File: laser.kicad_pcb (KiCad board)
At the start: 2 copper layers, 74 x 32 mm, 40 parts, among them J1 Conn_01x04_Socket, J2 Conn_02x04_Counter_Clockwise, J3 Conn_01x02_Pin, J4 Conn_01x02_Socket, J5 Conn_01x01_Pin, J6 Conn_01x01_Pin, J7 Conn_01x01_Pin, J8 Conn_01x01_Pin, J9 Conn_01x01_Pin, U1 MCP6002-xP

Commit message: Updated PCB board
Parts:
- D1, D2: moved to B.Cu
- moved R1 138.7 mm to (158.7, 89.4), turned to -90 degrees
- moved R12 131.8 mm to (162.1, 96.8)
- moved R2 120.6 mm to (133.9, 101.9), turned to 180 degrees
- moved C11 118.0 mm to (149.3, 119.7)
- moved D2 111.6 mm to (163.7, 90.0)
- moved R3 108.6 mm to (122.2, 101.9), turned to 180 degrees
- moved J2 103.2 mm to (154.0, 82.0), turned to -90 degrees
- moved J1 98.4 mm to (146.4, 95.0), turned to 90 degrees
- moved C4 97.1 mm to (126.2, 89.9), turned to -90 degrees
- moved C3 96.5 mm to (118.6, 95.3), turned to 90 degrees
- moved C2 78.8 mm to (131.4, 80.0), turned to 180 degrees
- moved U1 75.6 mm to (139.3, 69.3), turned to 90 degrees
- moved C1 74.0 mm to (120.1, 80.2), turned to 180 degrees
- moved D1 69.0 mm to (132.7, 90.0)
- moved J9 67.7 mm to (76.9, 116.6)
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
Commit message: Updated PCB
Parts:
- moved R6 118.8 mm to (174.3, 104.4)
- moved R10 102.9 mm to (153.8, 137.2), turned to 180 degrees
- moved R11 95.9 mm to (141.8, 151.2)
- moved C10 94.1 mm to (154.4, 145.8), turned to -90 degrees
- moved C6 90.2 mm to (165.4, 104.3)
- moved J9 89.0 mm to (164.5, 101.0)
- moved R8 88.6 mm to (134.3, 137.4), turned to 180 degrees
- moved R9 73.8 mm to (119.1, 138.2), turned to 180 degrees
- moved J8 68.2 mm to (145.9, 132.0)
- moved J7 65.6 mm to (91.4, 138.6)
- moved C9 64.5 mm to (97.8, 132.8)
- moved J4 64.4 mm to (164.6, 95.5)
- moved C8 60.4 mm to (127.9, 133.0)
- moved C13 52.1 mm to (127.7, 127.3)
- moved R7 40.7 mm to (65.3, 130.3), turned to 180 degrees
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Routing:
- added copper zone on F.Cu, net GND

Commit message: Connect all cables
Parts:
- moved R13 93.2 mm to (157.9, 103.5)
- moved J7 91.4 mm to (176.0, 104.0)
- moved C7 91.4 mm to (155.0, 97.0), turned to -90 degrees
- moved R7 90.8 mm to (152.0, 103.3), turned to 90 degrees
- moved R5 87.9 mm to (142.0, 104.1), turned to 90 degrees
- moved C12 81.8 mm to (171.5, 103.0), turned to 90 degrees
- moved C9 74.1 mm to (164.5, 100.5), turned to 180 degrees
- moved C10 69.5 mm to (141.5, 77.5)
- moved C5 65.8 mm to (138.0, 98.0), turned to -90 degrees
- moved R8 64.9 mm to (171.9, 84.5)
- moved R4 64.9 mm to (116.5, 103.8), turned to 90 degrees
- moved R11 64.8 mm to (138.5, 86.5), turned to -90 degrees
- moved C8 64.2 mm to (165.5, 81.0)
- moved C13 62.6 mm to (165.6, 77.5)
- moved R9 57.0 mm to (158.5, 97.0), turned to 0 degrees
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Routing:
- net GND: track 0.00 -> 120.8 mm
- net Net-(J6-Pin_1): track 0.00 -> 77.5 mm
- net +3.3V: track 0.00 -> 76.3 mm
- net /vgnd: track 0.00 -> 72.4 mm
- net Net-(D2-A): track 0.00 -> 49.7 mm
- net Net-(J8-Pin_1): track 0.00 -> 48.5 mm
- net Net-(J7-Pin_1): track 0.00 -> 46.5 mm
- net Net-(U1A--): track 0.00 -> 27.8 mm
- net Net-(U1B--): track 0.00 -> 24.9 mm
- net /rx: track 0.00 -> 14.8 mm
- net Net-(J2-Pin_4): track 0.00 -> 14.7 mm
- net Net-(C12-Pad2): track 0.00 -> 13.9 mm
- net Net-(J2-Pin_8): track 0.00 -> 12.9 mm
- net /tx: track 0.00 -> 12.6 mm
- net Net-(C10-Pad1): track 0.00 -> 10.5 mm
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
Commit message: Add GND to both sides
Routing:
- added copper zone on B.Cu, net GND
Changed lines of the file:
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@@
-	)
-	(gr_rect
-		(start 106.9 71.2)
-		(end 187.8 110.2)
-		(stroke
-			(width 0.2)
-			(type solid)
-		)
-		(fill no)
-		(layer "F.Cu")
-		(net "GND")
 	)
 	(gr_rect
@@
 		(layer "F.Cu")
 		(hatch edge 0.5)
+		(priority 1)
 		(connect_pads
 			(clearance 0.5)
 		)
 		(min_thickness 0.25)
-		(fill
+		(fill yes
 			(thermal_gap 0.5)
 			(thermal_bridge_width 0.5)
@@
 			)
 		)
+	)
+	(zone
+		(net "GND")
+		(layer "F.Cu")
+		(hatch edge 0.5)
+		(connect_pads
+			(clearance 0.5)
+		)
+		(min_thickness 0.25)
+		(fill yes
+			(thermal_gap 0.5)
+			(thermal_bridge_width 0.5)
+			(island_removal_mode 0)
+		)
+		(polygon
+			(pts
+				(xy 106.9 71.2) (xy 187.8 71.2) (xy 187.8 110.2) (xy 106.9 110.2)
+			)
+		)
+	)
+	(zone
+		(net "GND")
+		(layer "B.Cu")
+		(hatch edge 0.5)
+		(priority 2)
+		(connect_pads
+			(clearance 0.5)
+		)
+		(min_thickness 0.25)
+		(fill yes
+			(thermal_gap 0.5)
+			(thermal_bridge_width 0.5)
+			(island_removal_mode 0)
+		)
+		(polygon
+			(pts
+				(xy 104.5 69.5) (xy 189.5 69.5) (xy 189.5 112) (xy 104.5 112)
+			)
+		)

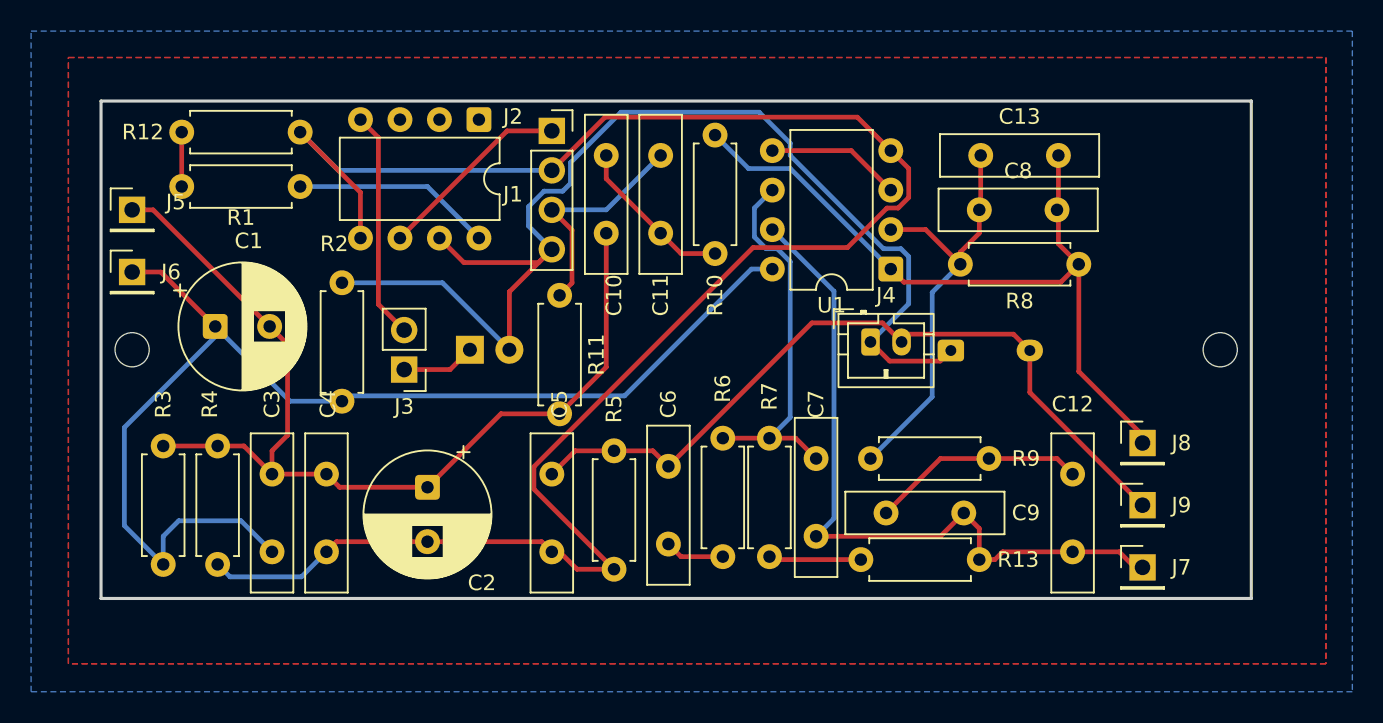
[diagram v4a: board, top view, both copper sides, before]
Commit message: Fix errors and warnings
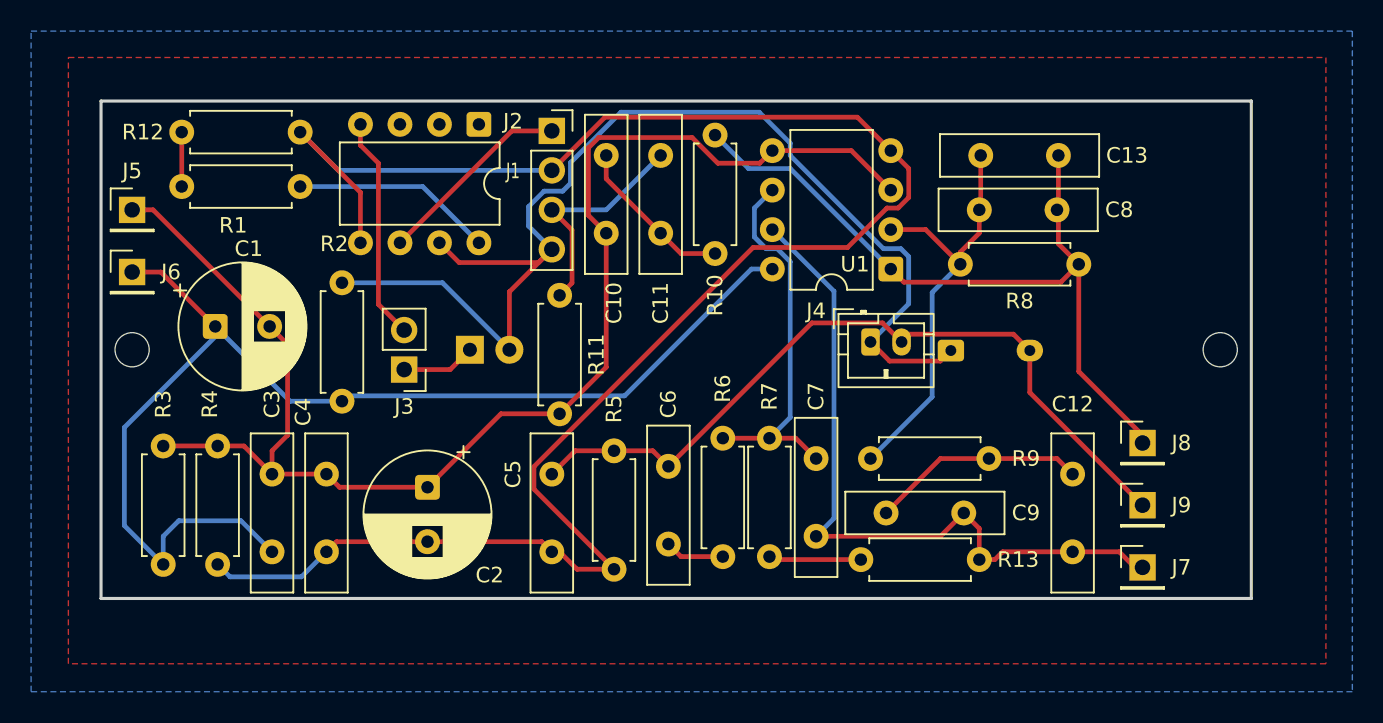
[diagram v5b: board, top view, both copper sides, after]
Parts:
- moved J2 0.31 mm to (133.3, 75.5)
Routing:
- net /vgnd: track 72.4 -> 91.5 mm
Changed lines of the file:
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@@
 	)
 	(setup
+		(stackup
+			(layer "F.SilkS"
+				(type "Top Silk Screen")
+			)
+			(layer "F.Paste"
+				(type "Top Solder Paste")
+			)
+			(layer "F.Mask"
+				(type "Top Solder Mask")
+				(thickness 0.01)
+			)
+			(layer "F.Cu"
+				(type "copper")
+				(thickness 0.035)
+			)
+			(layer "dielectric 1"
+				(type "core")
+				(thickness 1.51)
+				(material "FR4")
+				(epsilon_r 4.5)
+				(loss_tangent 0.02)
+			)
+			(layer "B.Cu"
+				(type "copper")
+				(thickness 0.035)
+			)
+			(layer "B.Mask"
+				(type "Bottom Solder Mask")
+				(thickness 0.01)
+			)
+			(layer "B.Paste"
+				(type "Bottom Solder Paste")
+			)
+			(layer "B.SilkS"
+				(type "Bottom Silk Screen")
+			)
+			(copper_finish "None")
+			(dielectric_constraints no)
+		)
 		(pad_to_mask_clearance 0)
 		(allow_soldermask_bridges_in_footprints no)
@@
 		(tags "C Disc series Radial pin pitch 5.00mm diameter 10mm width 2.5mm Capacitor")
 		(property "Reference" "C13"
-			(at 2.5 -2.5 0)
+			(at 9.41 0 0)
 			(layer "F.SilkS")
 			(effects
@@
 		(tags "CP Radial series Radial pin pitch 3.50mm diameter 8mm height 12mm Electrolytic Capacitor")
 		(property "Reference" "C2"
-			(at 6.152651 -3.5 180)
+			(at 5.652651 -4 180)
 			(layer "F.SilkS")
 			(effects
@@
 		(tags "CP Radial series Radial pin pitch 3.50mm diameter 8mm height 12mm Electrolytic Capacitor")
 		(property "Reference" "C1"
-			(at 2.152651 -5.5 0)
+			(at 2.152651 -5 0)
 			(layer "F.SilkS")
 			(effects
@@
 		(tags "C Disc series Radial pin pitch 5.00mm diameter 10mm width 2.5mm Capacitor")
 		(property "Reference" "C10"
-			(at 9 -0.5 90)
+			(at 9.5 -0.5 90)
 			(layer "F.SilkS")
 			(effects
@@
 		(tags "Resistor Axial_DIN0207 series Axial Horizontal pin pitch 7.62mm 0.25W = 1/4W length 6.3mm diameter 2.5mm")
 		(property "Reference" "R1"
-			(at 3.81 -2 0)
+			(at 4.31 -2.5 0)
 			(layer "F.SilkS")
 			(effects
@@
 		(tags "C Disc series Radial pin pitch 5.00mm diameter 10mm width 2.5mm Capacitor")
 		(property "Reference" "C4"
-			(at -4.5 -0.1 90)
+			(at -4 1.5 90)
 			(layer "F.SilkS")
 			(effects
@@
 		(tags "C Disc series Radial pin pitch 5.00mm diameter 10mm width 2.5mm Capacitor")
 		(property "Reference" "C5"
-			(at -4.5 -0.5 90)
+			(at 0 2.5 90)
 			(layer "F.SilkS")
 			(effects
@@
 		(tags "Through hole pin header THT 1x01 2.54mm single row")
 		(property "Reference" "J5"
-			(at 2.81 -0.5 0)
+			(at 0 -2.5 0)
 			(layer "F.SilkS")
 			(effects
@@
 		(tags "connector JST PH vertical")
 		(property "Reference" "J4"
-			(at 1 -3 0)
+			(at -3.5 -2 0)
 			(layer "F.SilkS")
 			(effects
@@
 		(tags "C Disc series Radial pin pitch 5.00mm diameter 10mm width 2.5mm Capacitor")
 		(property "Reference" "C8"
-			(at 2.5 -2.5 0)
+			(at 9 0 0)
 			(layer "F.SilkS")
 			(effects
@@
 		(tags "Through hole socket strip THT 1x04 2.54mm single row")
 		(property "Reference" "J1"
-			(at -2.5 4.08 0)
+			(at -2.5 2.58 0)
 			(layer "F.SilkS")
 			(effects
 				(font
-					(size 1 1)
+					(size 1 0.7)
 					(thickness 0.15)
 				)
@@
 		(tags "C Disc series Radial pin pitch 5.00mm diameter 10mm width 2.5mm Capacitor")
 		(property "Reference" "C11"
-			(at -4 0 90)
+			(at -4.5 0 90)
 			(layer "F.SilkS")
 			(effects
@@
 		(tags "THT DIP DIL PDIP 2.54mm 7.62mm 300mil")
 		(property "Reference" "U1"
-			(at 3.81 -2.33 0)
+			(at 2.305 0.31 0)
 			(layer "F.SilkS")
 			(effects
@@
 	(footprint "Package_DIP:DIP-8_W7.62mm"
 		(layer "F.Cu")
-		(at 133.31 75.195 -90)
+		(at 133.31 75.5 -90)
 		(descr "8-lead though-hole mounted DIP package, row spacing 7.62mm (300 mils)")
 		(tags "THT DIP DIL PDIP 2.54mm 7.62mm 300mil")
@@
 		)
 		(point
-			(at 129.5 79.005)
+			(at 129.5 79.31)
 			(size 1.27)
 			(layer "F.Fab")
@@
 		(tags "C Disc series Radial pin pitch 5.00mm diameter 10mm width 2.5mm Capacitor")
 		(property "Reference" "C7"
-			(at -3.5 0 90)
+			(at -4 0 90)
 			(layer "F.SilkS")
 			(effects
@@
 	)
 	(segment
+		(start 141.5 82.5)
+		(end 140.3475 81.3475)
+		(width 0.305)
+		(layer "F.Cu")
+		(net "/vgnd")
+	)
+	(segment
+		(start 148.680118 78)
+		(end 151.375 78)
+		(width 0.305)
+		(layer "F.Cu")
+		(net "/vgnd")
+	)
+	(segment
+		(start 147.027618 76.3475)
+		(end 148.680118 78)
+		(width 0.305)
+		(layer "F.Cu")
+		(net "/vgnd")
+	)
+	(segment
+		(start 140.3475 77.022618)
+		(end 141.022618 76.3475)
+		(width 0.305)
+		(layer "F.Cu")
+		(net "/vgnd")
+	)
+	(segment
 		(start 138.5 94.12)
 		(end 141.5 91.12)
@@
 	)
 	(segment
+		(start 140.3475 81.3475)
+		(end 140.3475 77.022618)
+		(width 0.305)
+		(layer "F.Cu")
+		(net "/vgnd")
+	)
+	(segment
 		(start 157.265 77.19)
 		(end 159.805 79.73)
@@
 	)
 	(segment
+		(start 151.375 78)
+		(end 152.185 77.19)
+		(width 0.305)
+		(layer "F.Cu")
+		(net "/vgnd")
+	)
+	(segment
+		(start 141.022618 76.3475)
+		(end 147.027618 76.3475)
+		(width 0.305)
+		(layer "F.Cu")
+		(net "/vgnd")
+	)
+	(segment
 		(start 141.5 91.12)
 		(end 141.5 82.5)
@@
 	)
 	(segment
-		(start 125.69 82.815)
-		(end 125.69 79.88)
-		(width 0.305)
-		(layer "F.Cu")
-		(net "GND")
-	)
-	(segment
 		(start 130 102.347349)
 		(end 124.152651 102.347349)
@@
 	)
 	(segment
+		(start 125.69 83.12)
+		(end 125.69 79.88)
+		(width 0.305)
+		(layer "F.Cu")
+		(net "GND")
+	)
+	(segment
 		(start 139.62 104.12)
 		(end 142 104.12)
@@
 	(segment
 		(start 121.81 79.5)
-		(end 129.995 79.5)
+		(end 129.69 79.5)
 		(width 0.305)
 		(layer "B.Cu")
@@
 	)
 	(segment
-		(start 129.995 79.5)
-		(end 133.31 82.815)
+		(start 133.31 83.12)
+		(end 129.69 79.5)
 		(width 0.305)
 		(layer "B.Cu")
@@
 	)
 	(segment
-		(start 132.345 84.39)
+		(start 132.04 84.39)
 		(end 137.15 84.39)
 		(width 0.305)
@@
 	)
 	(segment
+		(start 130.77 83.12)
+		(end 132.04 84.39)
+		(width 0.305)
+		(layer "F.Cu")
+		(net "+3.3V")
+	)
+	(segment
 		(start 159.7275 90.7275)
 		(end 162.9925 90.7275)
@@
 	)
 	(segment
-		(start 130.77 82.815)
-		(end 132.345 84.39)
-		(width 0.305)
-		(layer "F.Cu")
-		(net "+3.3V")
-	)
-	(segment
 		(start 137.15 84.39)
 		(end 138 83.54)
@@
 	)
 	(segment
-		(start 128.23 82.815)
-		(end 135.125 75.92)
+		(start 128.23 83.12)
+		(end 135.43 75.92)
 		(width 0.305)
 		(layer "F.Cu")
@@
 	)
 	(segment
-		(start 135.125 75.92)
+		(start 135.43 75.92)
 		(end 138 75.92)
 		(width 0.305)
@@
 	)
 	(segment
-		(start 126.8425 76.3475)
-		(end 125.69 75.195)
+		(start 125.69 75.5)
+		(end 125.69 76.8475)
 		(width 0.305)
 		(layer "F.Cu")
@@
 	(segment
 		(start 126.8425 87.0775)
-		(end 126.8425 76.3475)
+		(end 126.8425 78)
 		(width 0.305)
 		(layer "F.Cu")
@@
 	)
 	(segment
+		(start 125.69 76.8475)
+		(end 126.8425 78)
+		(width 0.305)
+		(layer "F.Cu")
+		(net "Net-(J2-Pin_4)")
+	)
+	(segment
 		(start 128.5 91.275)
 		(end 131.455 91.275)
@@
 		(connect_pads
 			(clearance 0.5)
-		)
-		(min_thickness 0.25)
-		(fill yes
-			(thermal_gap 0.5)
-			(thermal_bridge_width 0.5)
-			(island_removal_mode 0)
-		)
-		(polygon
-			(pts
-				(xy 106.9 71.2) (xy 187.8 71.2) (xy 187.8 110.2) (xy 106.9 110.2)
-			)
-		)
-	)
-	(zone
-		(net "GND")
-		(layer "F.Cu")
-		(hatch edge 0.5)
-		(connect_pads
-			(clearance 0.5)
